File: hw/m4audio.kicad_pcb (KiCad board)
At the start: 2 copper layers, 49.7 x 49.7 mm, 102 parts, among them J1 JACK_TRS, J11 CONN_01X03, J2 JACK_TRS, J21 CONN_01X03, P1 CONN_01X02, P2 USB_OTG, P3 CONN_02X05, P4 CONN_01X08, P5 CONN_01X03, P6 CONN_01X04, P7 CONN_01X02, P8 CONN_01X02, U1 AP2210K-3.3, U2 STM32F405RG, U3 AD8542, U4 WM8731, U5 AP2210K-3.3, Y1 Crystal

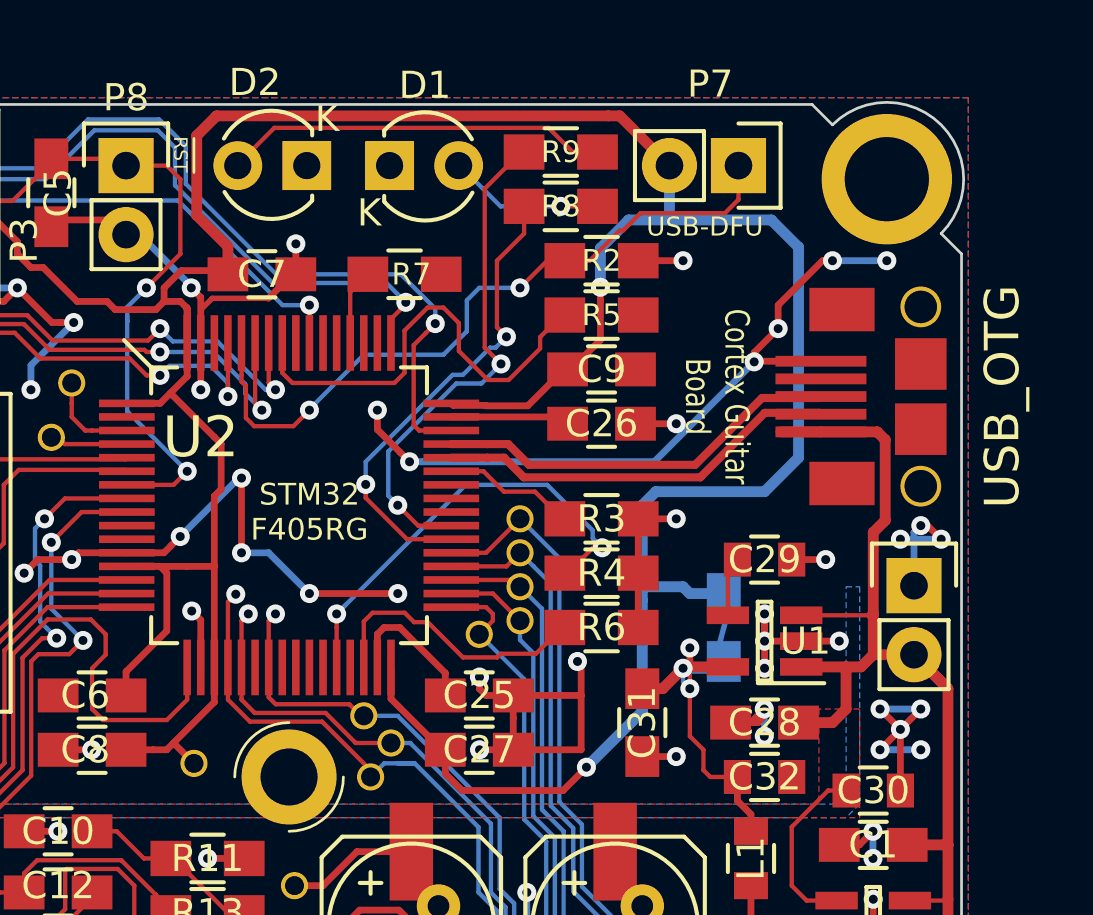
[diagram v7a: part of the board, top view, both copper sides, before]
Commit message: Tiny silk fixes
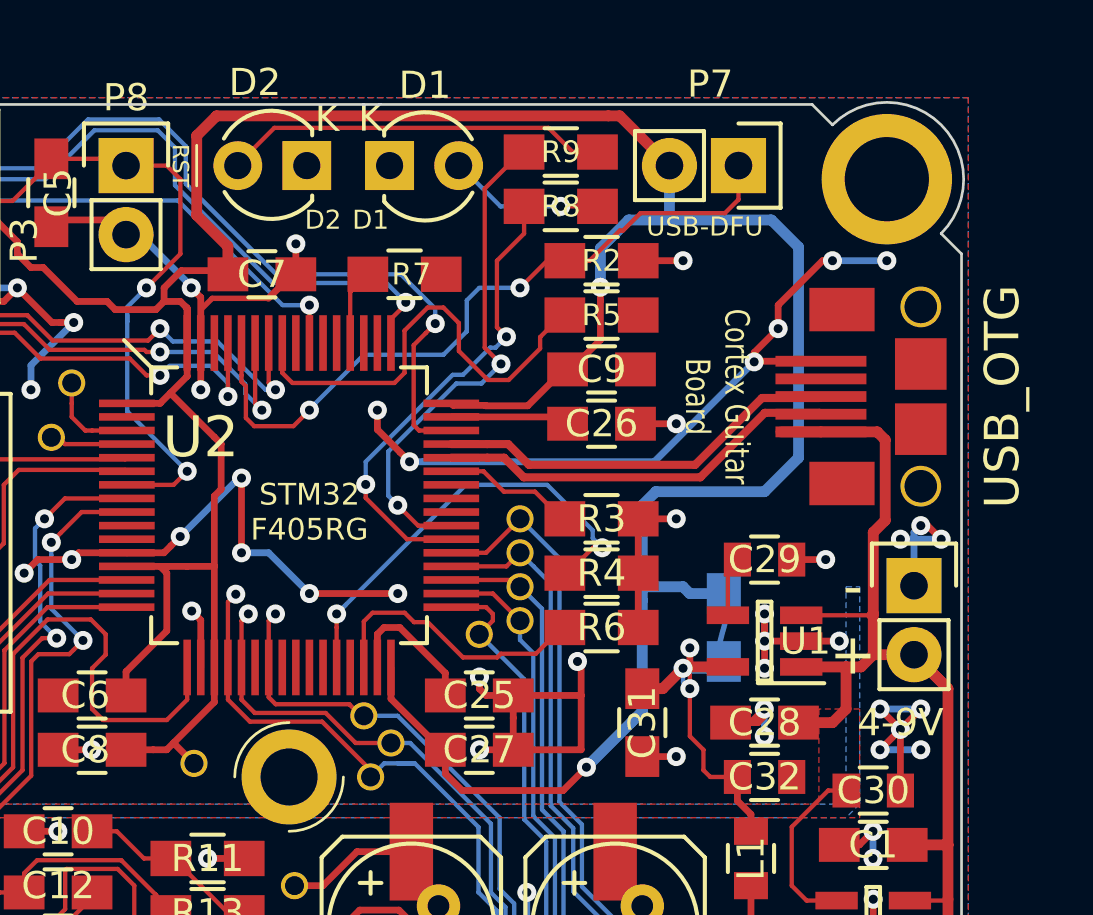
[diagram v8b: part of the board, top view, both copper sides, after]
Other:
- board text added: "+"
- board text added: "-"
- board text added: "4-9V"
- board text added: "D1"
- board text added: "D2"
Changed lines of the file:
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@@
   (general
     (links 204)
-    (no_connects 4)
+    (no_connects 0)
     (area 111.121572 90.121572 160.878428 139.878428)
     (thickness 1.6)
-    (drawings 148)
+    (drawings 153)
     (tracks 1275)
     (zones 0)
@@
     (35 F.Paste user hide)
     (36 B.SilkS user)
-    (37 F.SilkS user hide)
+    (37 F.SilkS user)
     (38 B.Mask user hide)
     (39 F.Mask user hide)
@@
     (fp_arc (start 1.301 0.034) (end -0.199 -1.286) (angle 108.5) (layer F.SilkS) (width 0.15))
     (fp_arc (start 1.311 0.034) (end 3.051 0.994) (angle 110) (layer F.SilkS) (width 0.15))
-    (fp_text user K (at -0.75 1.74) (layer F.SilkS)
+    (fp_text user K (at -0.7 -1.75) (layer F.SilkS)
       (effects (font (size 1 1) (thickness 0.15)))
     )
@@
       (net 7 /audio/AIN_R))
   )
+  (gr_text 4-9V (at 158.5 113) (layer F.SilkS)
+    (effects (font (size 1 1) (thickness 0.2)))
+  )
+  (gr_text + (at 156.75 110.5) (layer F.SilkS)
+    (effects (font (size 1.5 1.5) (thickness 0.3)))
+  )
+  (gr_text - (at 156.75 108) (layer F.SilkS)
+    (effects (font (size 1.5 1.5) (thickness 0.3)))
+  )
+  (gr_text D1 (at 139 94.5) (layer F.SilkS)
+    (effects (font (size 0.7 0.7) (thickness 0.1)))
+  )
+  (gr_text D2 (at 137.25 94.5) (layer F.SilkS)
+    (effects (font (size 0.7 0.7) (thickness 0.1)))
+  )
   (gr_text jack (at 128.75 130.25) (layer B.SilkS)
     (effects (font (size 1 1) (thickness 0.2)) (justify right mirror))
@@
     (effects (font (size 0.8 0.7) (thickness 0.15)))
   )
-  (gr_line (start 131.25 91) (end 131.25 93) (layer B.SilkS) (width 0.1))
-  (gr_text RST (at 132 92 90) (layer B.SilkS)
+  (gr_line (start 131.25 91.5) (end 131.25 93.5) (layer B.SilkS) (width 0.1))
+  (gr_text RST (at 132 92.5 90) (layer B.SilkS)
     (effects (font (size 0.8 0.7) (thickness 0.1)) (justify mirror))
   )
-  (gr_text GND (at 132 94.5 90) (layer B.SilkS)
+  (gr_text GND (at 132 95 90) (layer B.SilkS)
     (effects (font (size 0.8 0.7) (thickness 0.1)) (justify mirror))
   )
@@
     (effects (font (size 0.8 0.8) (thickness 0.15)))
   )
-  (gr_line (start 132.5 92.75) (end 132.5 91.5) (layer F.SilkS) (width 0.1))
-  (gr_text RST (at 132 92.75 270) (layer F.SilkS)
-    (effects (font (size 0.5 0.5) (thickness 0.1)) (justify right))
+  (gr_line (start 132.6 93.25) (end 132.6 91.75) (layer F.SilkS) (width 0.1))
+  (gr_text RST (at 132 92.5 270) (layer F.SilkS)
+    (effects (font (size 0.6 0.6) (thickness 0.1)))
   )
   (gr_text VMID (at 155.75 134) (layer B.SilkS)
